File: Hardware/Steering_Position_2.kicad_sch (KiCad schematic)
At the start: 11 parts, among them U10 MCP6001-OT, U23 MCP6001-OT

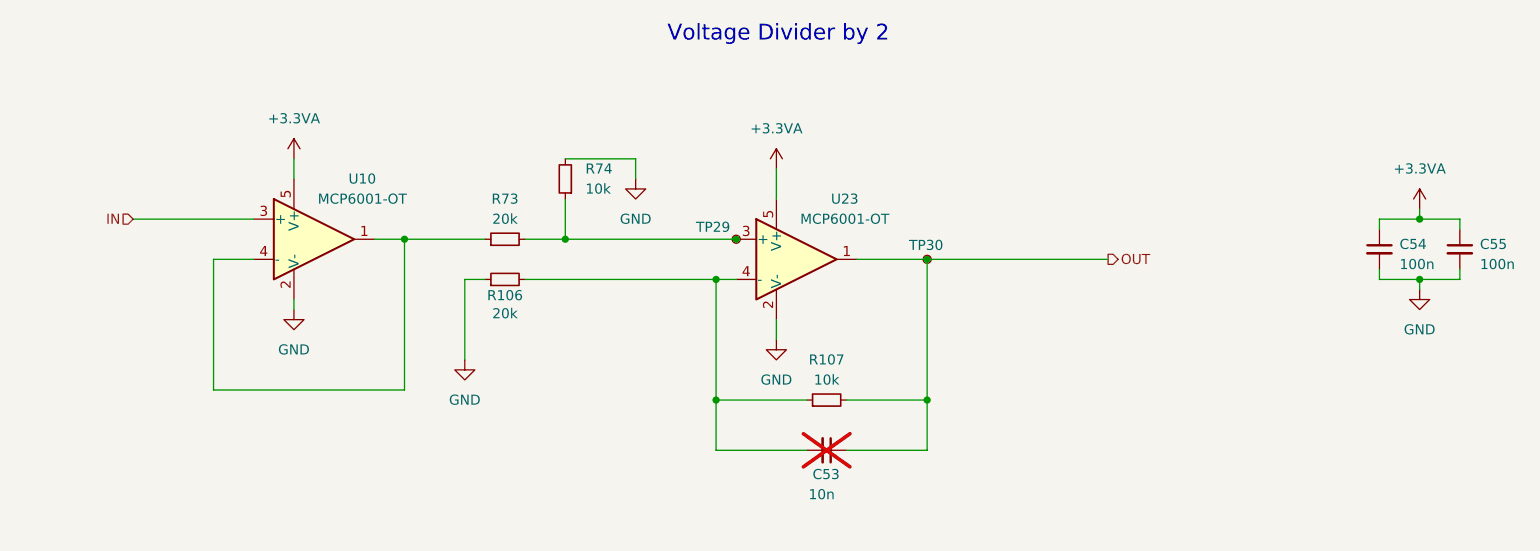
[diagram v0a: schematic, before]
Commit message: Changes for new steering position system
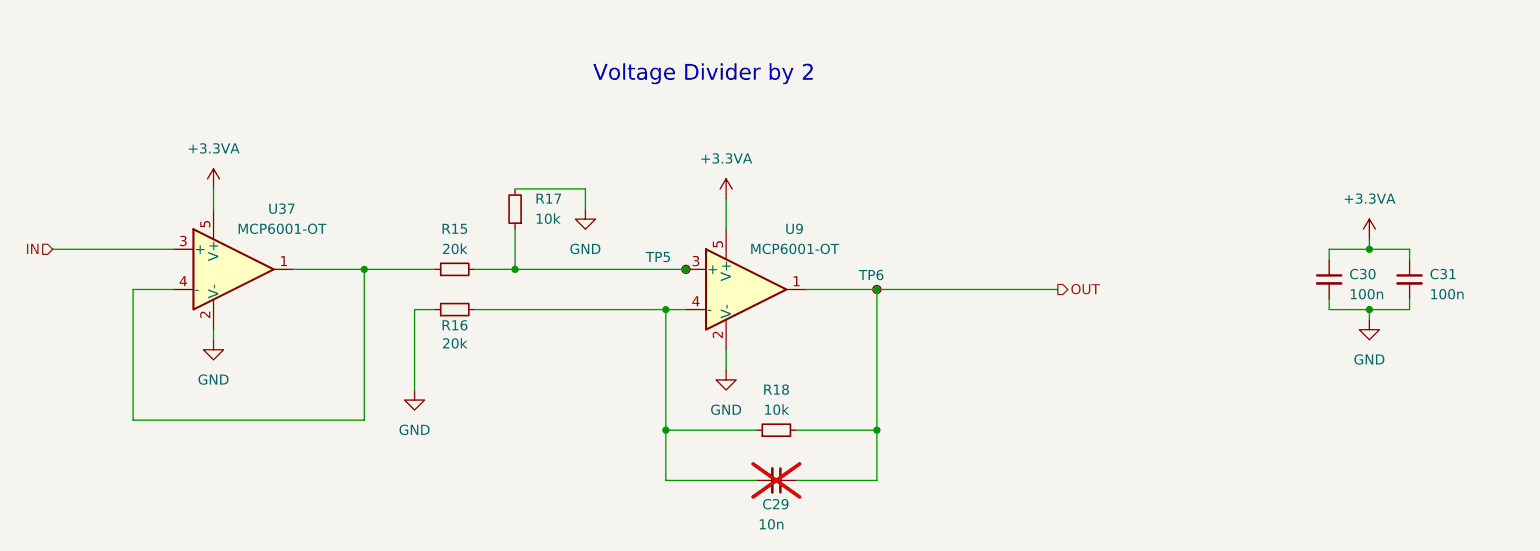
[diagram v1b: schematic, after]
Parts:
- removed C53: 10n, Capacitor_SMD:C_0603_1608Metric, symbol Device:C_Small
- removed C54, C55: 100n, Capacitor_SMD:C_0603_1608Metric, symbol Device:C_Small
- removed R106, R73: 20k, Resistor_SMD:R_0603_1608Metric, symbol Device:R_Small
- removed R107, R74: 10k, Resistor_SMD:R_0603_1608Metric, symbol Device:R_Small
- removed TP29, TP30: TestPoint_Small, TestPoint:TestPoint_Pad_D1.0mm, symbol Connector:TestPoint_Small
- removed U10, U23: MCP6001-OT, Package_TO_SOT_SMD:SOT-23-5, symbol Amplifier_Operational:MCP6001-OT
- added C29: 10n, Capacitor_SMD:C_0603_1608Metric, symbol Device:C_Small
- added C30, C31: 100n, Capacitor_SMD:C_0603_1608Metric, symbol Device:C_Small
- added R15, R16: 20k, Resistor_SMD:R_0603_1608Metric, symbol Device:R_Small
- added R17, R18: 10k, Resistor_SMD:R_0603_1608Metric, symbol Device:R_Small
- added TP5, TP6: TestPoint_Small, TestPoint:TestPoint_Pad_D1.0mm, symbol Connector:TestPoint_Small
- added U37, U9: MCP6001-OT, Package_TO_SOT_SMD:SOT-23-5, symbol Amplifier_Operational:MCP6001-OT
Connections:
- net +3.3VA: now also C30.1, C31.1, U37.5 (V+), U9.5 (V+)
- net GND: now also C30.2, C31.2, R16.1, R17.2, U37.2 (V-), U9.2 (V-)
- net IN: now also U37.3 (+)
- net OUT: now also C29.1, R18.2, TP6.1, U9.1
- new net: R15.2, R17.1, TP5.1, U9.3 (+)
- new net: R15.1, U37.1, U37.4 (-)
- new net: C29.2, R16.2, R18.1, U9.4 (-)

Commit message: Changes in power section
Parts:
- TP5, TP6: footprint TestPoint:TestPoint_Pad_D1.0mm -> TestPoint:TestPoint_THTPad_D1.0mm_Drill0.5mm
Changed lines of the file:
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@@
 			)
 		)
-		(property "Footprint" "TestPoint:TestPoint_Pad_D1.0mm"
+		(property "Footprint" "TestPoint:TestPoint_THTPad_D1.0mm_Drill0.5mm"
 			(at 133.35 85.09 0)
 			(effects
@@
 			)
 		)
-		(property "Footprint" "TestPoint:TestPoint_Pad_D1.0mm"
+		(property "Footprint" "TestPoint:TestPoint_THTPad_D1.0mm_Drill0.5mm"
 			(at 157.48 87.63 0)
 			(effects

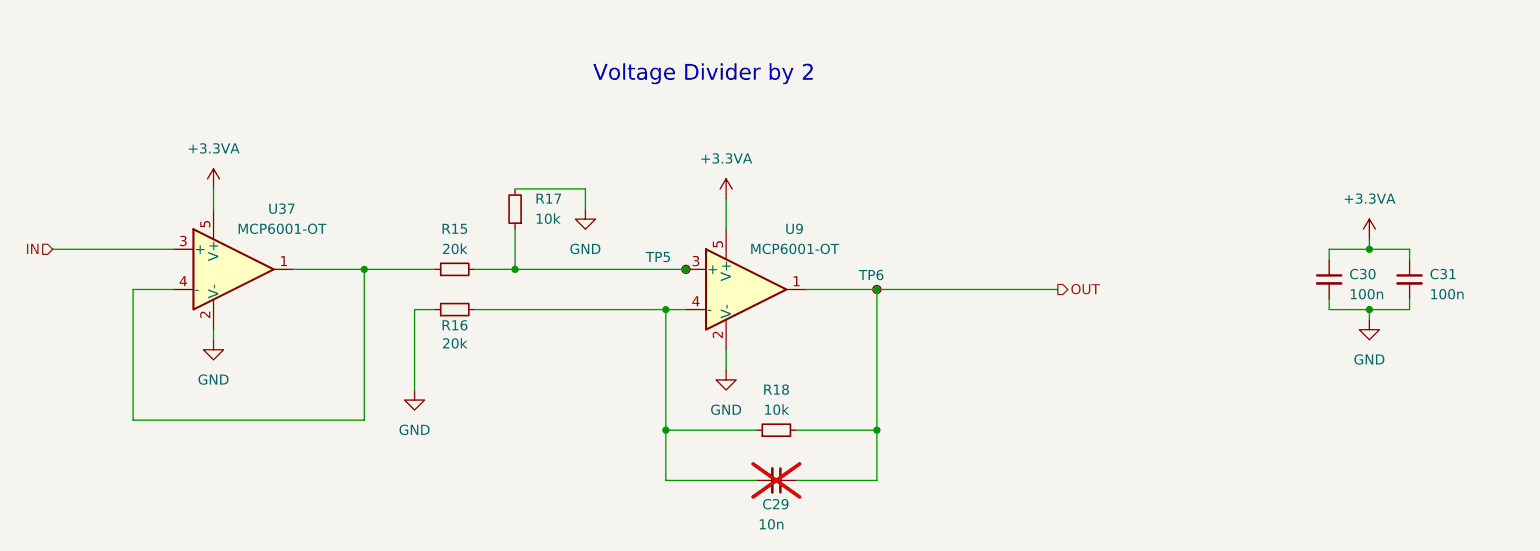
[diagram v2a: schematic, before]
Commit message: Changes Vcc op-amps in brakes pressure (3V3 to 5V) and mcp6002 footprint (to MSOP8)
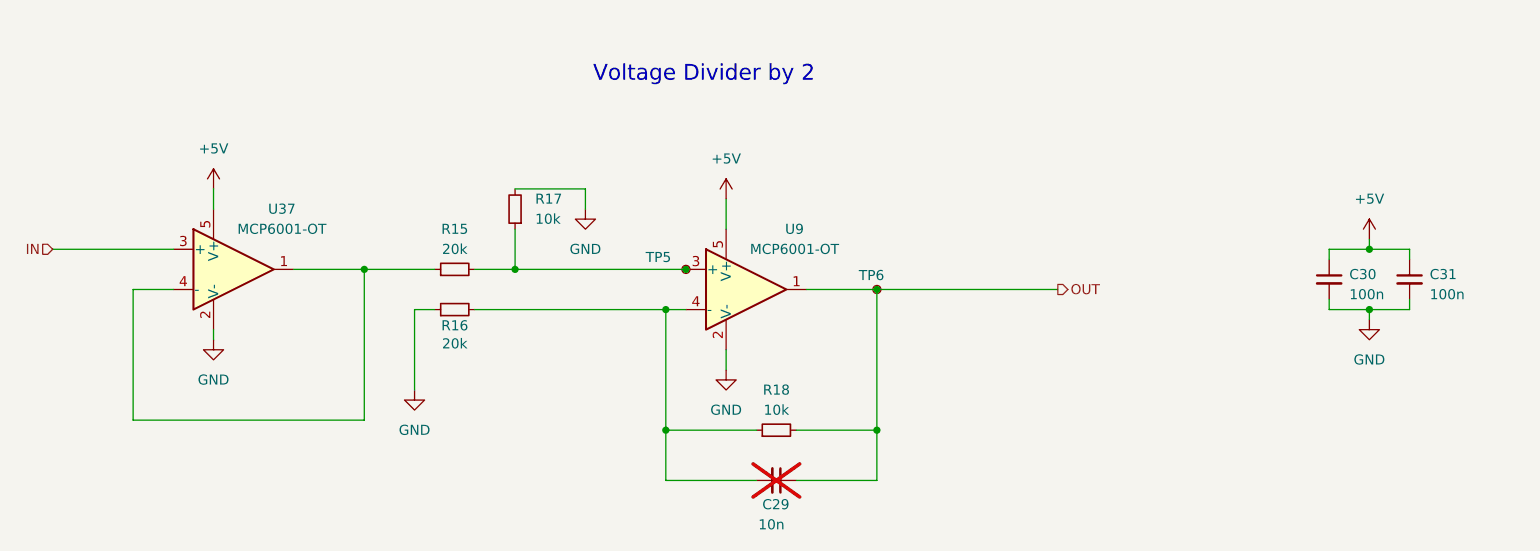
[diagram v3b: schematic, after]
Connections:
- net +3.3VA renamed +5V
